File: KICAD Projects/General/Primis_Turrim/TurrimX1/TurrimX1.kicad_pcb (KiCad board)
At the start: 2 copper layers, 49 x 28 mm, 8 parts, among them J1 USB_C_Receptacle_USB2.0_16P, J2 USB_A

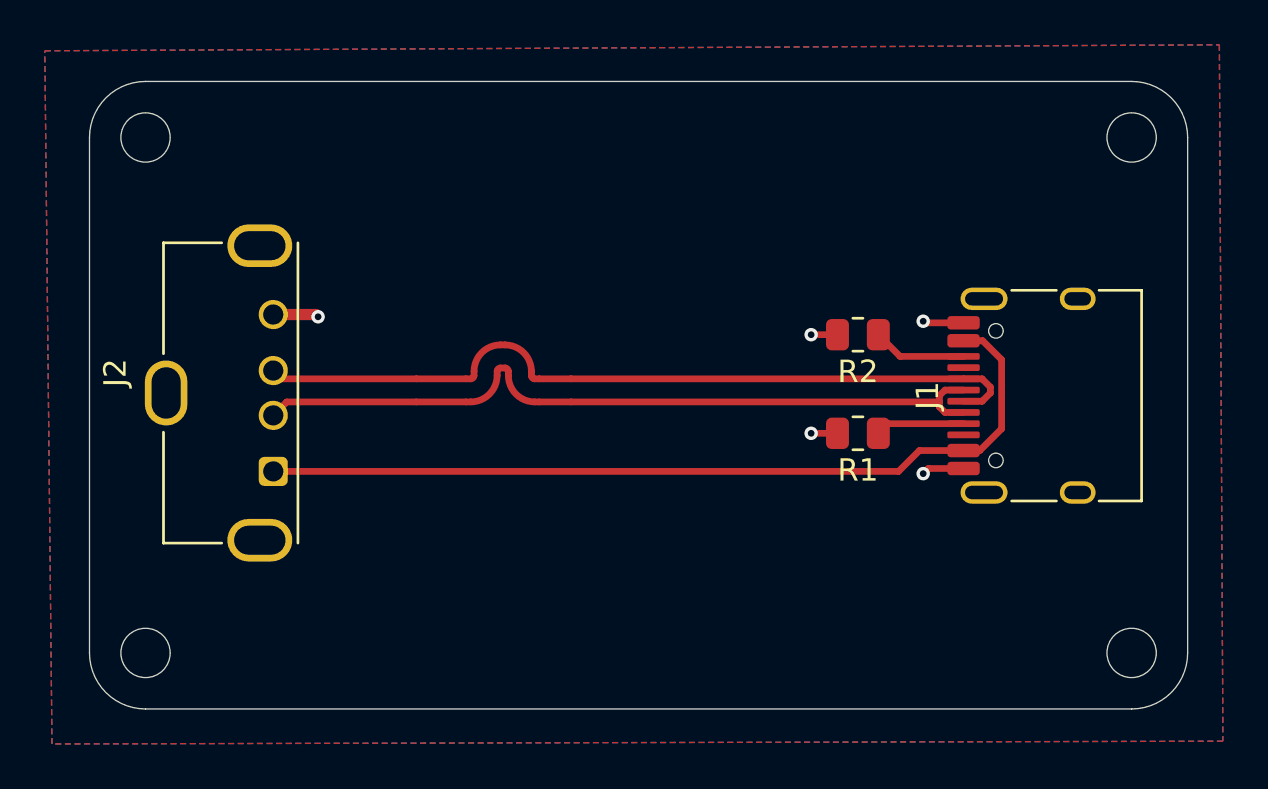
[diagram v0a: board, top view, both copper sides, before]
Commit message: VERSIPELLIS EV2 + TURRIM Production files
-Swapped to a tag connect for programming VERSIPELLIS
-Moved crystal closer to the NRF on VERSIPELLIS
-Fixed swapped lines on usb on VERSIPELLIS
-TURRIM cleanup and production files added
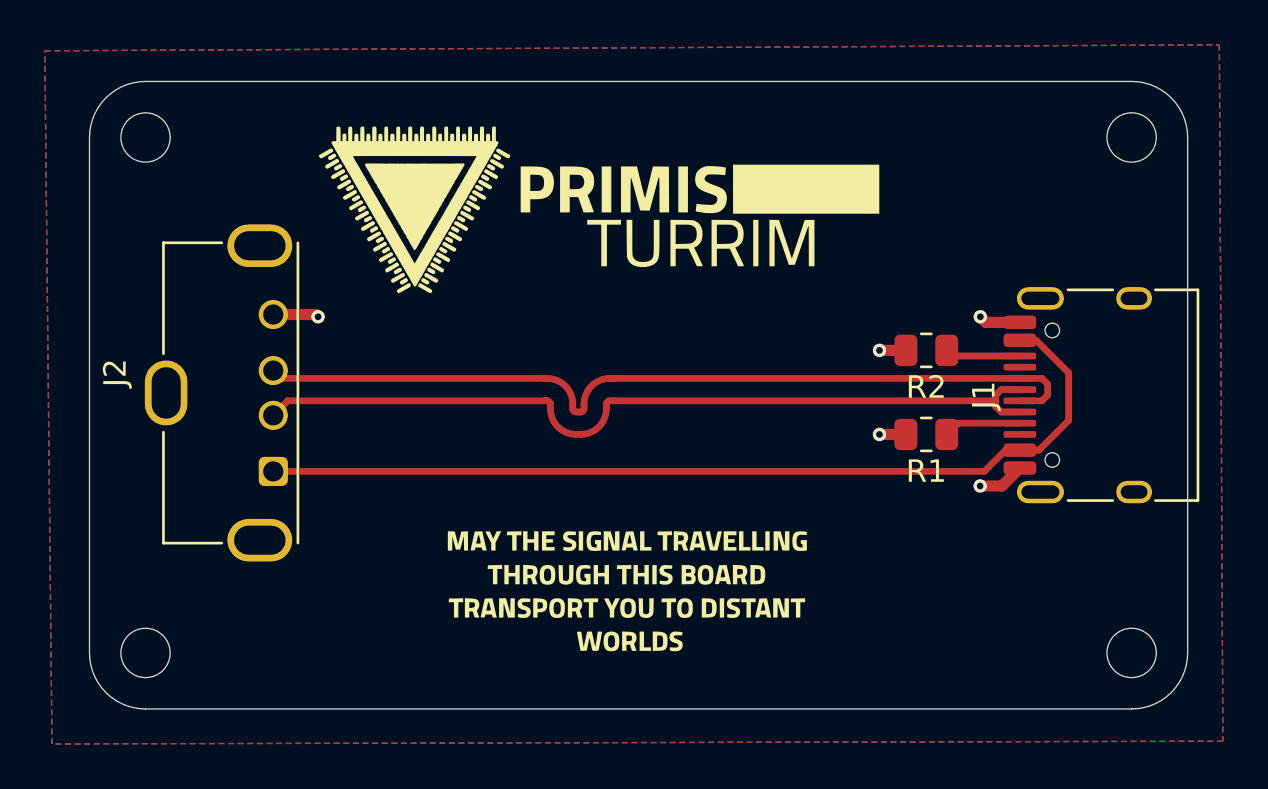
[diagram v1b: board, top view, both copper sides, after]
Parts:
- added G***: LOGO, LOGO, F.Cu at (141.0, 108.2)
- added G***: LOGO, LOGO, F.Cu at (144.2, 91.5)
- added G***: LOGO, LOGO, F.Cu at (131.5, 91.2)
- moved R2 3.13 mm to (154.3, 97.5)
- moved R1 3.05 mm to (154.3, 101.2)
- moved J1 2.52 mm to (162.6, 99.5)
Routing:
- net Net-(J2-VBUS): track 38.4 -> 41.3 mm
- net D+: track 35.7 -> 38.4 mm
- net D-: track 34.6 -> 37.1 mm
- net Net-(J1-CC2): track 4.20 -> 3.37 mm
- net Net-(J1-CC1): track 3.98 -> 3.47 mm
